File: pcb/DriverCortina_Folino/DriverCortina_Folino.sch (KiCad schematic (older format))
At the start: 34 parts, among them J1 AC 220v, J2 Llave Inversora, J3 Motor 1, J4 Motor 2, K1 G3MB-202PL-DC5, K2 G3MB-202PL-DC5, Q1 BC558, Q2 BC558, U1 ESP-01v090

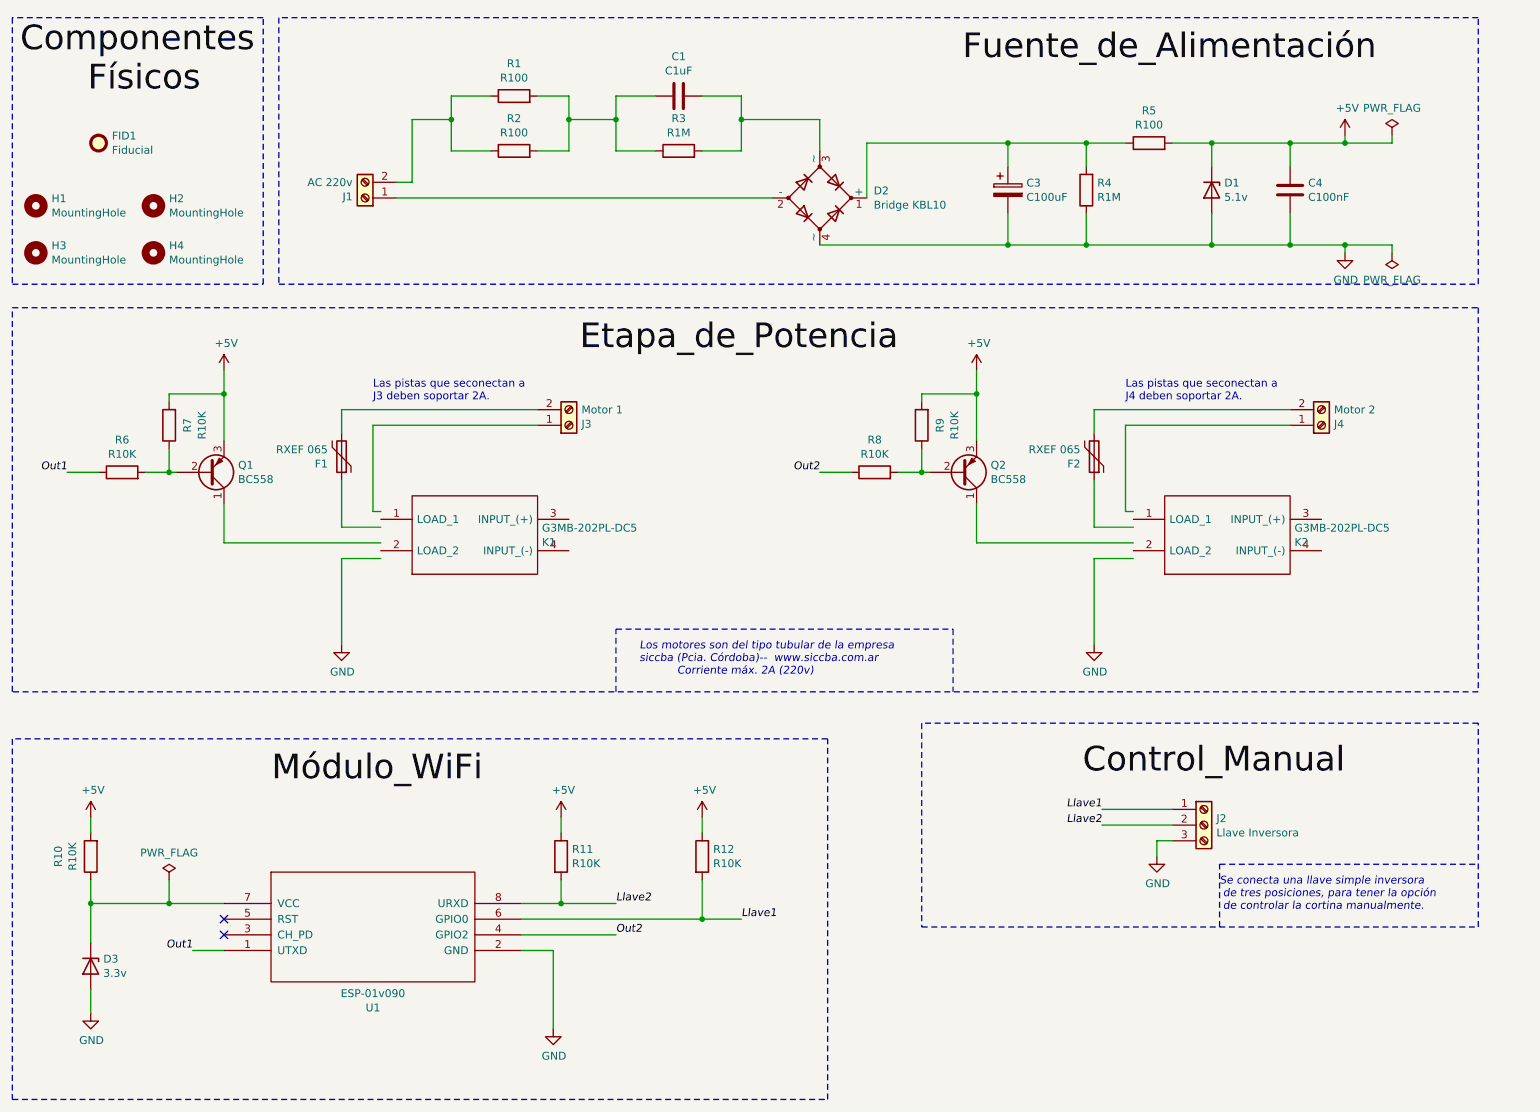
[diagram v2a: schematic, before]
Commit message: Creación PCB y modelo 3D de SSR
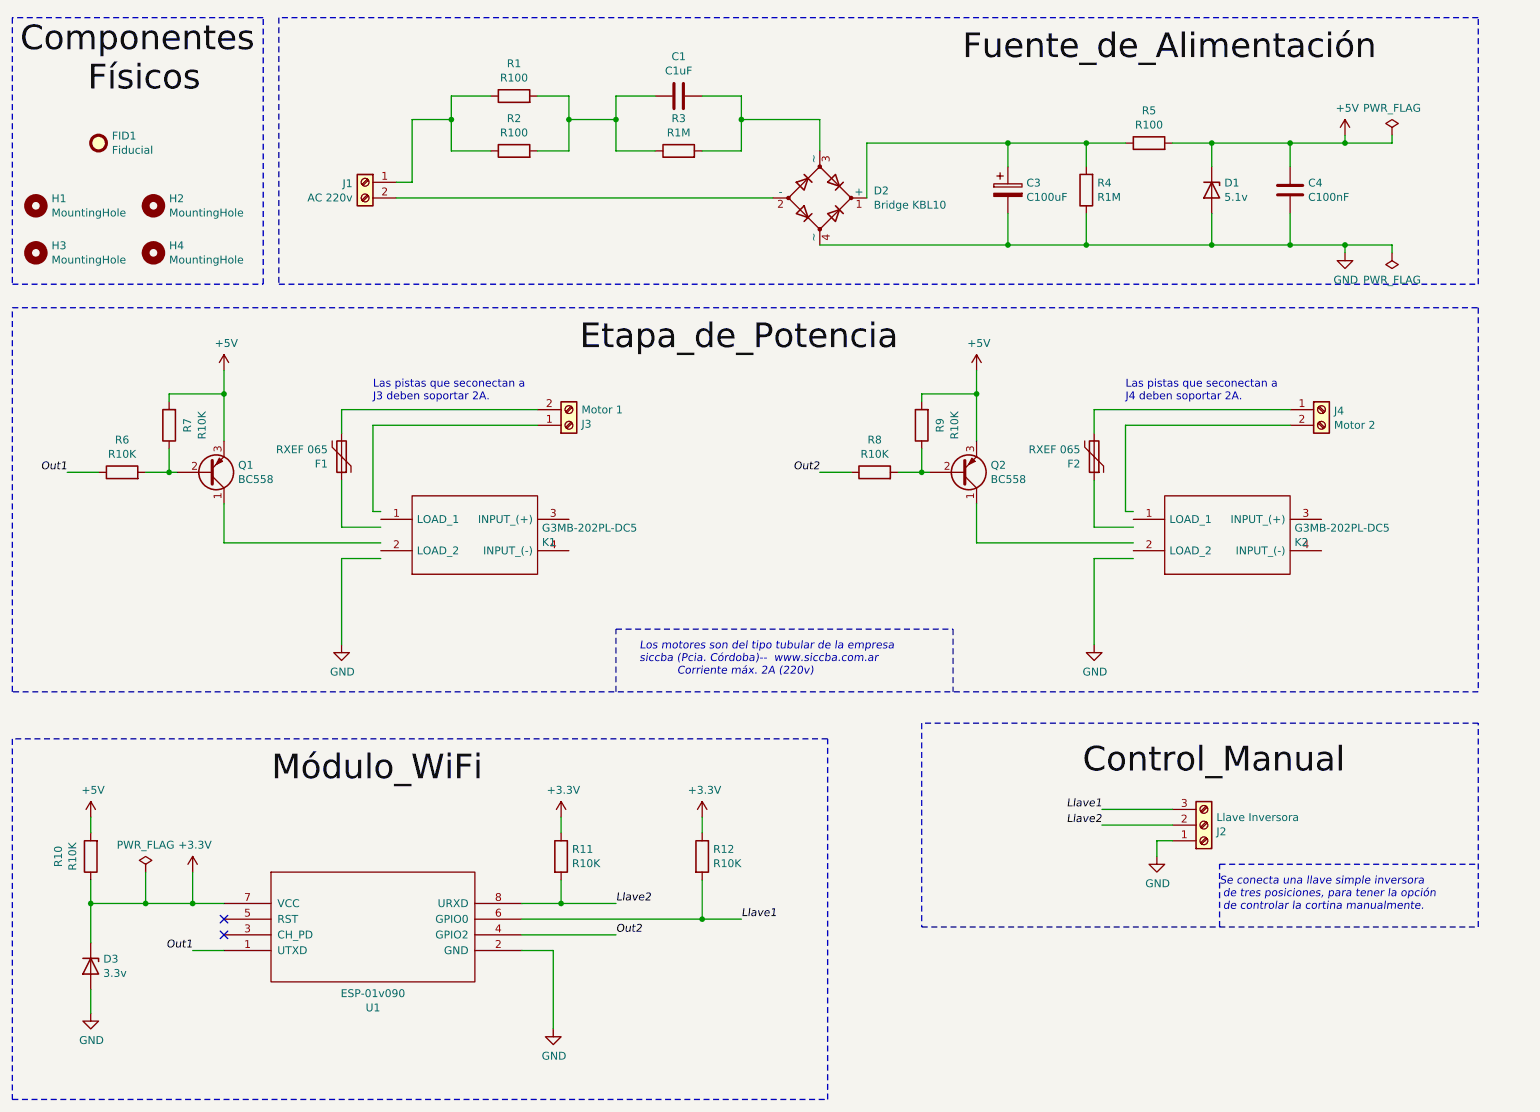
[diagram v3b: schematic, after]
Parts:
- Q1: footprint Package_TO_SOT_THT:TO-92L_Inline -> Package_TO_SOT_THT:TO-92L_Inline_Wide
- R1, R10, R11, R12, R2, R3, R4, R5, R6, R7, R8, R9: footprint Resistor_THT:R_Axial_DIN0207_L6.3mm_D2.5mm_P2.54mm_Vertical -> Resistor_THT:R_Axial_DIN0207_L6.3mm_D2.5mm_P10.16mm_Horizontal
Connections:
- net labels added: +3.3V
- wire segments 110 -> 112
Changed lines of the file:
@@
 Rev "1.2"
 Comp "CESE_FIUBA"
-Comment1 "Revisor: Ing. Sergio Alberino"
-Comment2 "Autor: Ing. Pablo D. Folino"
-Comment3 ""
+Comment1 "Profesor: Diego Brengi"
+Comment2 "Revisor: Ing. Sergio Alberino"
+Comment3 "Autor: Ing. Pablo D. Folino"
 Comment4 ""
 $EndDescr
@@
 F 0 "R1" V 4557 1200 50  0000 C CNN
 F 1 "R100" V 4466 1200 50  0000 C CNN
-F 2 "Resistor_THT:R_Axial_DIN0207_L6.3mm_D2.5mm_P2.54mm_Vertical" V 4280 1200 50  0001 C CNN
+F 2 "Resistor_THT:R_Axial_DIN0207_L6.3mm_D2.5mm_P10.16mm_Horizontal" V 4280 1200 50  0001 C CNN
 F 3 "~" H 4350 1200 50  0001 C CNN
 F 4 "1/4 w" H 4350 1200 50  0001 C CNN "Description"
@@
 F 0 "R2" V 4557 1550 50  0000 C CNN
 F 1 "R100" V 4466 1550 50  0000 C CNN
-F 2 "Resistor_THT:R_Axial_DIN0207_L6.3mm_D2.5mm_P2.54mm_Vertical" V 4280 1550 50  0001 C CNN
+F 2 "Resistor_THT:R_Axial_DIN0207_L6.3mm_D2.5mm_P10.16mm_Horizontal" V 4280 1550 50  0001 C CNN
 F 3 "~" H 4350 1550 50  0001 C CNN
 F 4 "1/4 w" H 4350 1550 50  0001 C CNN "Description"
@@
 F 0 "R3" V 5607 1550 50  0000 C CNN
 F 1 "R1M" V 5516 1550 50  0000 C CNN
-F 2 "Resistor_THT:R_Axial_DIN0207_L6.3mm_D2.5mm_P2.54mm_Vertical" V 5330 1550 50  0001 C CNN
+F 2 "Resistor_THT:R_Axial_DIN0207_L6.3mm_D2.5mm_P10.16mm_Horizontal" V 5330 1550 50  0001 C CNN
 F 3 "~" H 5400 1550 50  0001 C CNN
 F 4 "1/4 w" H 5400 1550 50  0001 C CNN "Description"
@@
 F 0 "R5" V 8607 1500 50  0000 C CNN
 F 1 "R100" V 8516 1500 50  0000 C CNN
-F 2 "Resistor_THT:R_Axial_DIN0207_L6.3mm_D2.5mm_P2.54mm_Vertical" V 8330 1500 50  0001 C CNN
+F 2 "Resistor_THT:R_Axial_DIN0207_L6.3mm_D2.5mm_P10.16mm_Horizontal" V 8330 1500 50  0001 C CNN
 F 3 "~" H 8400 1500 50  0001 C CNN
 F 4 "1/4 w" H 8400 1500 50  0001 C CNN "Description"
@@
 L Connector:Screw_Terminal_01x02 J1
 U 1 1 60477EAA
-P 3400 1850
-F 0 "J1" H 3480 1842 50  0000 L CNN
-F 1 "AC 220v" H 3480 1751 50  0000 L CNN
-F 2 "DriverCortina_Folino:bornera_1x2_con_tornillo_5.08mm" H 3400 1850 50  0001 C CNN
-F 3 "~" H 3400 1850 50  0001 C CNN
-	1    3400 1850
-	-1   0    0    1
+P 3400 1750
+F 0 "J1" H 3480 1742 50  0000 L CNN
+F 1 "AC 220v" H 3480 1651 50  0000 L CNN
+F 2 "DriverCortina_Folino:bornera_1x2_con_tornillo_5.08mm" H 3400 1750 50  0001 C CNN
+F 3 "~" H 3400 1750 50  0001 C CNN
+	1    3400 1750
+	-1   0    0    -1
 $EndComp
 $Comp
@@
 F 0 "R4" H 7930 1754 50  0000 R CNN
 F 1 "R1M" H 7930 1845 50  0000 R CNN
-F 2 "Resistor_THT:R_Axial_DIN0207_L6.3mm_D2.5mm_P2.54mm_Vertical" V 7930 1800 50  0001 C CNN
+F 2 "Resistor_THT:R_Axial_DIN0207_L6.3mm_D2.5mm_P10.16mm_Horizontal" V 7930 1800 50  0001 C CNN
 F 3 "~" H 8000 1800 50  0001 C CNN
 F 4 "1/4 w" H 8000 1800 50  0001 C CNN "Description"
@@
 F 0 "R10" V 1857 6050 50  0000 C CNN
 F 1 "R10K" V 1766 6050 50  0000 C CNN
-F 2 "Resistor_THT:R_Axial_DIN0207_L6.3mm_D2.5mm_P2.54mm_Vertical" V 1580 6050 50  0001 C CNN
+F 2 "Resistor_THT:R_Axial_DIN0207_L6.3mm_D2.5mm_P10.16mm_Horizontal" V 1580 6050 50  0001 C CNN
 F 3 "~" H 1650 6050 50  0001 C CNN
 F 4 "1/4 w" H 1650 6050 50  0001 C CNN "Description"
@@
 F 0 "Q1" H 2590 3554 50  0000 L CNN
 F 1 "BC558" H 2590 3645 50  0000 L CNN
-F 2 "Package_TO_SOT_THT:TO-92L_Inline" H 2600 3700 50  0001 C CNN
+F 2 "Package_TO_SOT_THT:TO-92L_Inline_Wide" H 2600 3700 50  0001 C CNN
 F 3 "~" H 2400 3600 50  0001 C CNN
 F 4 "Transistor PNP" H 2400 3600 50  0001 C CNN "Description"
@@
 F 0 "R6" V 2057 3600 50  0000 C CNN
 F 1 "R10K" V 1966 3600 50  0000 C CNN
-F 2 "Resistor_THT:R_Axial_DIN0207_L6.3mm_D2.5mm_P2.54mm_Vertical" V 1780 3600 50  0001 C CNN
+F 2 "Resistor_THT:R_Axial_DIN0207_L6.3mm_D2.5mm_P10.16mm_Horizontal" V 1780 3600 50  0001 C CNN
 F 3 "~" H 1850 3600 50  0001 C CNN
 F 4 "1/4 w" H 1850 3600 50  0001 C CNN "Description"
@@
 F 3 "~" H 8750 5850 50  0001 C CNN
 	1    8750 5850
-	1    0    0    -1
+	1    0    0    1
 $EndComp
 $Comp
@@
 F 0 "R11" H 4720 6096 50  0000 L CNN
 F 1 "R10K" H 4720 6005 50  0000 L CNN
-F 2 "Resistor_THT:R_Axial_DIN0207_L6.3mm_D2.5mm_P2.54mm_Vertical" V 4580 6050 50  0001 C CNN
+F 2 "Resistor_THT:R_Axial_DIN0207_L6.3mm_D2.5mm_P10.16mm_Horizontal" V 4580 6050 50  0001 C CNN
 F 3 "~" H 4650 6050 50  0001 C CNN
 F 4 "1/4 w" H 4650 6050 50  0001 C CNN "Description"
@@
 F 0 "R12" H 5620 6096 50  0000 L CNN
 F 1 "R10K" H 5620 6005 50  0000 L CNN
-F 2 "Resistor_THT:R_Axial_DIN0207_L6.3mm_D2.5mm_P2.54mm_Vertical" V 5480 6050 50  0001 C CNN
+F 2 "Resistor_THT:R_Axial_DIN0207_L6.3mm_D2.5mm_P10.16mm_Horizontal" V 5480 6050 50  0001 C CNN
 F 3 "~" H 5550 6050 50  0001 C CNN
 F 4 "1/4 w" H 5550 6050 50  0001 C CNN "Description"
@@
 	5550 6450 5800 6450
 Connection ~ 4650 6350
-$Comp
-L power:+5V #PWR0109
-U 1 1 606A3869
-P 4650 5800
-F 0 "#PWR0109" H 4650 5650 50  0001 C CNN
-F 1 "+5V" H 4665 5973 50  0000 C CNN
-F 2 "" H 4650 5800 50  0001 C CNN
-F 3 "" H 4650 5800 50  0001 C CNN
-	1    4650 5800
-	1    0    0    -1
-$EndComp
-$Comp
-L power:+5V #PWR0110
-U 1 1 606A4477
-P 5550 5800
-F 0 "#PWR0110" H 5550 5650 50  0001 C CNN
-F 1 "+5V" H 5565 5973 50  0000 C CNN
-F 2 "" H 5550 5800 50  0001 C CNN
-F 3 "" H 5550 5800 50  0001 C CNN
-	1    5550 5800
-	1    0    0    -1
-$EndComp
 Wire Wire Line
 	4650 5800 4650 5900
@@
 F 0 "R7" V 2004 3300 50  0000 C TNN
 F 1 "R10K" V 1911 3300 50  0000 C TNN
-F 2 "Resistor_THT:R_Axial_DIN0207_L6.3mm_D2.5mm_P2.54mm_Vertical" V 2080 3300 50  0001 C CNN
+F 2 "Resistor_THT:R_Axial_DIN0207_L6.3mm_D2.5mm_P10.16mm_Horizontal" V 2080 3300 50  0001 C CNN
 F 3 "~" H 2150 3300 50  0001 C CNN
 F 4 "1/4 w" H 2150 3300 50  0001 C CNN "Description"
@@
 L Connector:Screw_Terminal_01x02 J4
 U 1 1 6074D5D9
-P 9500 3300
-F 0 "J4" H 9580 3292 50  0000 L CNN
-F 1 "Motor 2" H 9580 3201 50  0000 L CNN
-F 2 "DriverCortina_Folino:bornera_1x2_con_tornillo_5.08mm" H 9500 3300 50  0001 C CNN
-F 3 "~" H 9500 3300 50  0001 C CNN
-	1    9500 3300
-	1    0    0    1
+P 9500 3200
+F 0 "J4" H 9580 3192 50  0000 L CNN
+F 1 "Motor 2" H 9580 3101 50  0000 L CNN
+F 2 "DriverCortina_Folino:bornera_1x2_con_tornillo_5.08mm" H 9500 3200 50  0001 C CNN
+F 3 "~" H 9500 3200 50  0001 C CNN
+	1    9500 3200
+	1    0    0    -1
 $EndComp
 $Comp
@@
 F 0 "R8" V 6857 3600 50  0000 C CNN
 F 1 "R10K" V 6766 3600 50  0000 C CNN
-F 2 "Resistor_THT:R_Axial_DIN0207_L6.3mm_D2.5mm_P2.54mm_Vertical" V 6580 3600 50  0001 C CNN
+F 2 "Resistor_THT:R_Axial_DIN0207_L6.3mm_D2.5mm_P10.16mm_Horizontal" V 6580 3600 50  0001 C CNN
 F 3 "~" H 6650 3600 50  0001 C CNN
 F 4 "1/4 w" H 6650 3600 50  0001 C CNN "Description"
@@
 F 0 "R9" V 6804 3300 50  0000 C TNN
 F 1 "R10K" V 6711 3300 50  0000 C TNN
-F 2 "Resistor_THT:R_Axial_DIN0207_L6.3mm_D2.5mm_P2.54mm_Vertical" V 6880 3300 50  0001 C CNN
+F 2 "Resistor_THT:R_Axial_DIN0207_L6.3mm_D2.5mm_P10.16mm_Horizontal" V 6880 3300 50  0001 C CNN
 F 3 "~" H 6950 3300 50  0001 C CNN
 F 4 "1/4 w" H 6950 3300 50  0001 C CNN "Description"
@@
 Wire Wire Line
 	1650 6200 1650 6350
-Wire Wire Line
-	2500 6350 2150 6350
 NoConn ~ 2500 6450
 NoConn ~ 2500 6550
@@
 L power:PWR_FLAG #FLG0103
 U 1 1 6070AA25
-P 2150 6200
-F 0 "#FLG0103" H 2150 6275 50  0001 C CNN
-F 1 "PWR_FLAG" H 2150 6373 50  0000 C CNN
-F 2 "" H 2150 6200 50  0001 C CNN
-F 3 "~" H 2150 6200 50  0001 C CNN
-	1    2150 6200
-	1    0    0    -1
-$EndComp
-Wire Wire Line
-	2150 6200 2150 6350
-Connection ~ 2150 6350
-Wire Wire Line
-	2150 6350 1650 6350
+P 2000 6150
+F 0 "#FLG0103" H 2000 6225 50  0001 C CNN
+F 1 "PWR_FLAG" H 2000 6323 50  0000 C CNN
+F 2 "" H 2000 6150 50  0001 C CNN
+F 3 "~" H 2000 6150 50  0001 C CNN
+	1    2000 6150
+	1    0    0    -1
+$EndComp
 $Comp
 L Mechanical:Fiducial FID1
@@
 Wire Wire Line
 	1650 6900 1650 7050
+$Comp
+L power:+3.3V #PWR0109
+U 1 1 60733302
+P 2300 6150
+F 0 "#PWR0109" H 2300 6000 50  0001 C CNN
+F 1 "+3.3V" H 2315 6323 50  0000 C CNN
+F 2 "" H 2300 6150 50  0001 C CNN
+F 3 "" H 2300 6150 50  0001 C CNN
+	1    2300 6150
+	1    0    0    -1
+$EndComp
+$Comp
+L power:+3.3V #PWR0110
+U 1 1 60735F80
+P 4650 5800
+F 0 "#PWR0110" H 4650 5650 50  0001 C CNN
+F 1 "+3.3V" H 4665 5973 50  0000 C CNN
+F 2 "" H 4650 5800 50  0001 C CNN
+F 3 "" H 4650 5800 50  0001 C CNN
+	1    4650 5800
+	1    0    0    -1
+$EndComp
+$Comp
+L power:+3.3V #PWR0113
+U 1 1 60737B56
+P 5550 5800
+F 0 "#PWR0113" H 5550 5650 50  0001 C CNN
+F 1 "+3.3V" H 5565 5973 50  0000 C CNN
+F 2 "" H 5550 5800 50  0001 C CNN
+F 3 "" H 5550 5800 50  0001 C CNN
+	1    5550 5800
+	1    0    0    -1
+$EndComp
+Wire Wire Line
+	1650 6350 2000 6350
+Wire Wire Line
+	2000 6150 2000 6350
+Connection ~ 2000 6350
+Wire Wire Line
+	2000 6350 2300 6350
+Wire Wire Line
+	2300 6150 2300 6350
+Connection ~ 2300 6350
+Wire Wire Line
+	2300 6350 2500 6350
 $EndSCHEMATC

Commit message: Se realizan las correciones del esquemático.
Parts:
- C1: value C1uF -> 1uF; Manufacturer_Name (none) -> Weidy; Manufacturer_Part_Number (none) -> W42Q3105-P8*******
- C3: value C100uF -> 100uF
- C4: value C100nF -> 100nF
- D1: Manufacturer_Name (none) -> Vishay Semiconductors; Manufacturer_Part_Number (none) -> BZX55C5V1
- D2: Manufacturer_Name (none) -> SEP ELECTRONIC CORP; Manufacturer_Part_Number (none) -> KBL10
- D3: Manufacturer_Name (none) -> Vishay Semiconductors; Manufacturer_Part_Number (none) -> BZX55C3V3
- F1, F2: value RXEF 065 -> RXEF065; Arrow Price/Stock Raychem -> (none)
- R1, R2, R5: value R100 -> 100
- R10, R11, R12, R6, R7, R8, R9: value R10K -> 10K
- R3, R4: value R1M -> 1M
- renumbered U1 to XU1
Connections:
- net labels removed: Componentes, Control_Manual, Etapa_de_Potencia, Fuente_de_Alimentación, Físicos, Módulo_WiFi
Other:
- note added: "Agujeros y\n fiduciales"
- note added: "Control_Manual"
- note added: "Etapa_de_Potencia"
- note added: "Fuente_de_Alimentación"
- note added: "Módulo_WiFi"
- moved on the sheet: F1, F2, J3, J4, K1, K2

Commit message: Se actualiza PCB
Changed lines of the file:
@@
 Text Notes 1300 1200 0    157  ~ 0
 Agujeros y\n fiduciales
+$Comp
+L Poncho_Esqueleto:OSHWA #G1
+U 1 1 607E3158
+P 9750 4600
+F 0 "#G1" H 9720 5000 60  0001 C CNN
+F 1 "OSHWA" H 9750 4903 60  0001 C CNN
+F 2 "" H 9750 4600 60  0000 C CNN
+F 3 "" H 9750 4600 60  0000 C CNN
+	1    9750 4600
+	1    0    0    -1
+$EndComp
 $EndSCHEMATC
